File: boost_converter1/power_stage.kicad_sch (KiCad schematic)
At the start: 7 parts, among them J2 Load, Q1 IRFP4468PbF

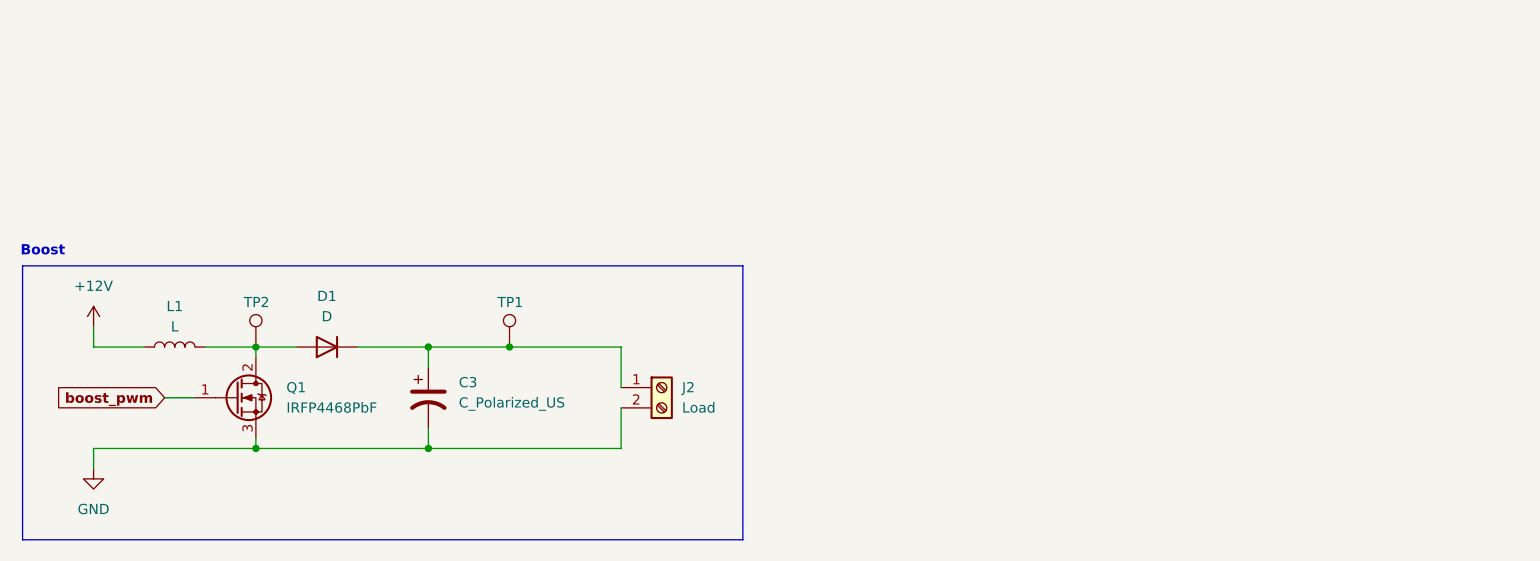
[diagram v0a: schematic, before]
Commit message: Updated components and footprints for power stage.
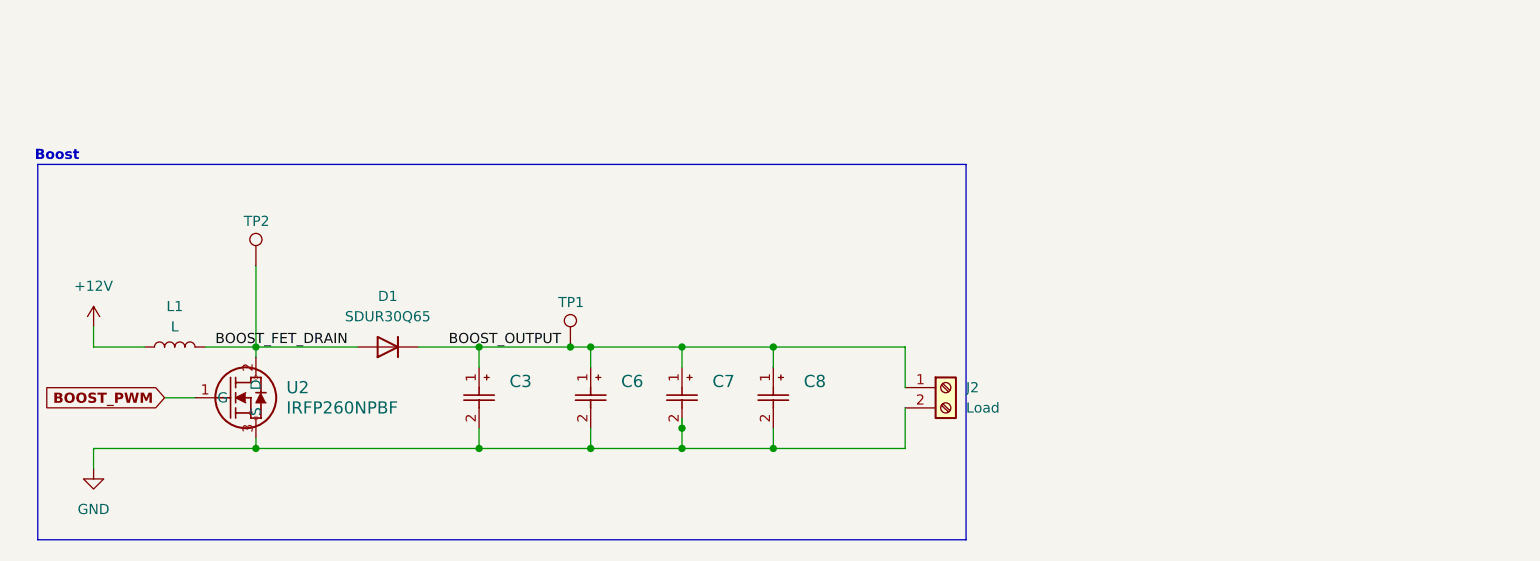
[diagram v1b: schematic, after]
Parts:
- removed C3: C_Polarized_US, symbol Device:C_Polarized_US
- removed Q1: IRFP4468PbF, Package_TO_SOT_THT:TO-247-3_Vertical, symbol Transistor_FET:IRFP4468PbF
- added C3, C6, C7, C8: UVZ2A331MHD1TO, CAP_UEP_12P5X25_NCH, symbol UVZ2A331MHD1TO:UVZ2A331MHD1TO
- added U2: IRFP260NPBF, PG-TO247-3-46_INF, symbol IRFP260N:IRFP260NPBF
- D1: value D -> SDUR30Q65; footprint (none) -> Package_TO_SOT_THT:TO-220-2_Vertical
- L1: footprint (none) -> iiks_footprints:200uHCustomL
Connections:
- net GND: now also C3.2, C6.2, C7.2, C8.2, U2.3 (S)
- net BOOST_FET_DRAIN: now reaches D1.2 (A), L1.2, TP2.1
- net BOOST_FET_DRAIN: now also U2.2 (D)
- net BOOST_OUTPUT: now reaches D1.1 (K), J2.1 (Pin_1), TP1.1
- net BOOST_OUTPUT: now also C3.1, C6.1, C7.1, C8.1
- new net BOOST_PWM: U2.1 (G)
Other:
- moved on the sheet: D1, J2, TP1, TP2

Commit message: [HW] Added MCU supporting components and programming connector.
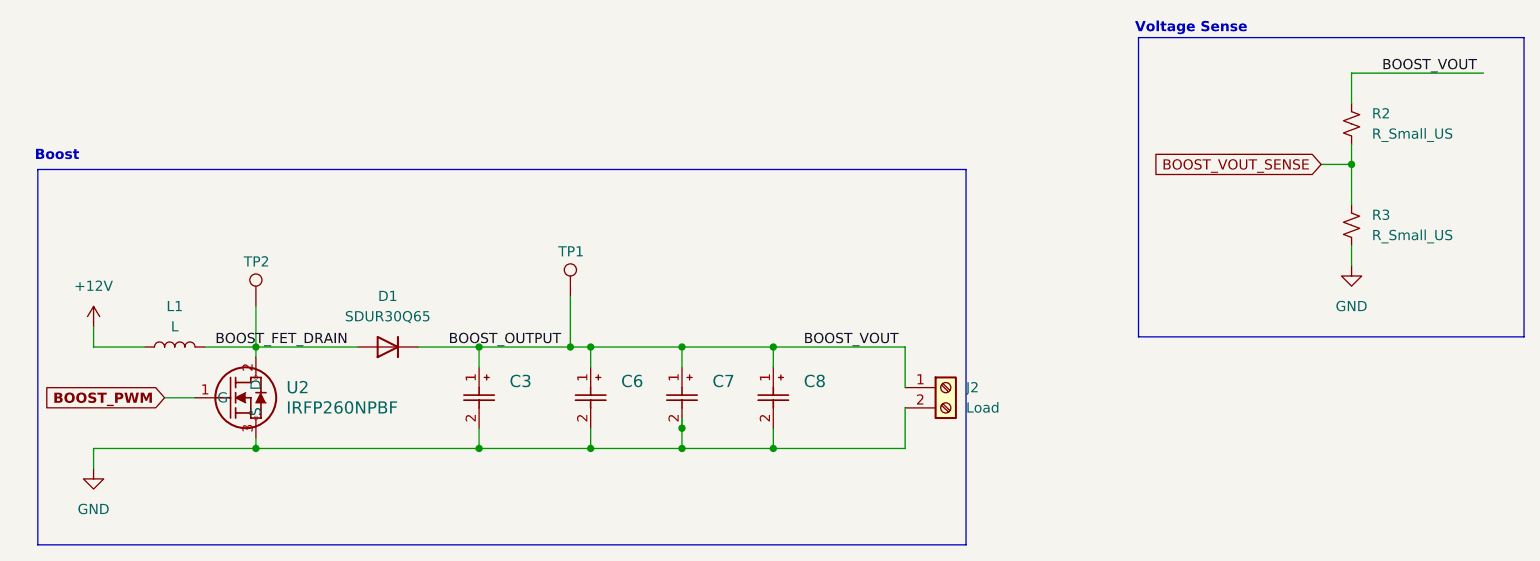
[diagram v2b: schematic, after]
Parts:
- added R2, R3: R_Small_US, symbol Device:R_Small_US
- TP1, TP2: footprint (none) -> TestPoint:TestPoint_THTPad_4.0x4.0mm_Drill2.0mm
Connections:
- net BOOST_OUTPUT: now also R2.1
- net GND: now also R3.2
- new net BOOST_VOUT_SENSE: R2.2, R3.1
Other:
- note added: "Voltage Sense"
- moved on the sheet: TP1
